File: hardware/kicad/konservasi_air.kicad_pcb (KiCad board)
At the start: 2 copper layers, 26 parts, among them J1 ADS1115, J10 PUMP, J11 DC_IN_TERMINAL, J2 DS18B20, J3 TDS, J4 TURBIDITY, J5 pH, J6 SERVO, J7 OLED, J8 ADS1115_ADDR_JP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

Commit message: PCB Layout Update
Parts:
- removed the SW1 at (66.0, 66.0)
- C1, C2: footprint Capacitor_THT:C_Disc_D7.5mm_W5.0mm_P7.50mm -> Capacitor_THT:C_Disc_D5.0mm_W2.5mm_P5.00mm
- D2: footprint Diode_THT:D_A-405_P12.70mm_Horizontal -> Diode_THT:D_DO-34_SOD68_P7.62mm_Horizontal
- J10: footprint Connector_PinSocket_2.54mm:PinSocket_1x02_P2.54mm_Vertical -> Connector_Molex:Molex_SL_171971-0002_1x02_P2.54mm_Vertical
- J8: value ADS1115_ADDR_JP -> ADS1115_ADDR
- R1, R2, R3, R4, R5: footprint Resistor_THT:R_Axial_DIN0309_L9.0mm_D3.2mm_P12.70mm_Horizontal -> Resistor_THT:R_Axial_DIN0204_L3.6mm_D1.6mm_P7.62mm_Horizontal
- SW1: renamed from SW2; footprint Connector_PinSocket_2.54mm:PinSocket_1x02_P2.54mm_Vertical -> Connector_Molex:Molex_SL_171971-0002_1x02_P2.54mm_Vertical
- moved J7 149.4 mm to (48.8, 118.6), turned to 90 degrees
- moved J6 143.2 mm to (48.8, 130.0), turned to 90 degrees
- moved D2 115.9 mm to (57.4, 135.9)
- moved Q1 98.2 mm to (60.8, 129.5)
- moved J4 78.4 mm to (119.7, 126.2), turned to -90 degrees
- moved J3 77.0 mm to (119.6, 114.6), turned to -90 degrees
- moved R5 74.8 mm to (66.0, 128.3), turned to -90 degrees
- moved J10 55.5 mm to (48.8, 138.9), turned to 90 degrees
- moved J11 53.0 mm to (63.2, 151.1), turned to 0 degrees
- moved SW1 45.1 mm to (48.8, 104.4), turned to 90 degrees
- moved R3 42.0 mm to (106.7, 115.3), turned to 90 degrees
- moved R4 41.0 mm to (109.0, 115.3), turned to 90 degrees
- moved C3 36.6 mm to (64.0, 140.7)
- moved C2 36.5 mm to (77.8, 151.6), turned to 0 degrees
- moved J9 36.3 mm to (50.6, 144.4)
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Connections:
- J8 pad 2: /ADS1115_ADDR -> GND
- J8 pad 4: /ADS1115_ADDR -> +5V
- J8 pad 5: GND -> /ADS1115_ADDR
- J8 pad 6: +5V -> /ADS1115_SDA
- J8 pad 7: /ADS1115_SDA -> /ADS1115_ADDR
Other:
- board outline added: 77.2 x 56.4 mm
- board text added: "OLED"
- board text added: "PH"
- board text added: "PUMP"
- board text added: "RESET"
- board text added: "SERVO"
- board text added: "TDS"
- board text added: "TEMP"
- board text added: "TURBIDITY"

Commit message: PCB Update
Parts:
- added J12: ESP_GPIO_LEFT, Connector_PinHeader_2.54mm:PinHeader_1x19_P2.54mm_Vertical, F.Cu at (68.6, 106.7)
- added J13: ESP_GPIO_RIGHT, Connector_PinHeader_2.54mm:PinHeader_1x19_P2.54mm_Vertical, F.Cu at (101.6, 106.7)
- moved R3 3.94 mm to (110.6, 115.6)
- moved R2 1.76 mm to (57.2, 145.8)
- moved D2 1.74 mm to (55.7, 135.9)
- moved C3 1.74 mm to (62.3, 140.7)
- moved C4 1.74 mm to (56.4, 140.7)
- moved D1 1.74 mm to (55.2, 151.9)
- moved J10 1.74 mm to (47.0, 138.9)
- moved J11 1.74 mm to (61.5, 151.1)
- moved J6 1.74 mm to (47.0, 130.0)
- moved J7 1.74 mm to (47.0, 118.6)
- moved J9 1.74 mm to (48.9, 144.4)
- moved Q1 1.74 mm to (59.0, 129.5)
- moved R5 1.74 mm to (64.3, 128.3)
- moved SW1 1.74 mm to (47.0, 104.4)
- moved R1 1.66 mm to (112.9, 108.0)
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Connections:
- net Net-(U1-CHIP_PU) renamed /ESP_RESET
- net Net-(U1-GPIO23) renamed /ESP_GPIO23
- U1 pad 10: unconnected-(U1-DAC_2/ADC2_CH9/GPIO26-Pad10) -> /ESP_GPIO26
- U1 pad 11: unconnected-(U1-ADC2_CH7/GPIO27-Pad11) -> /ESP_GPIO27
- U1 pad 12: unconnected-(U1-MTMS/GPIO14/ADC2_CH6-Pad12) -> /ESP_GPIO14
- U1 pad 13: unconnected-(U1-MTDI/GPIO12/ADC2_CH5-Pad13) -> /PUMP_DIGITAL
- U1 pad 15: unconnected-(U1-MTCK/GPIO13/ADC2_CH4-Pad15) -> /ESP_GPIO13
- U1 pad 16: unconnected-(U1-SD_DATA2/GPIO9-Pad16) -> /ESP_GPIO09
- U1 pad 17: unconnected-(U1-SD_DATA3/GPIO10-Pad17) -> /ESP_GPIO10
- U1 pad 18: unconnected-(U1-CMD-Pad18) -> /ESP_CMD
- U1 pad 20: unconnected-(U1-SD_CLK/GPIO6-Pad20) -> /ESP_GPIO06
- U1 pad 21: unconnected-(U1-SD_DATA0/GPIO7-Pad21) -> /ESP_GPIO07
- U1 pad 22: unconnected-(U1-SD_DATA1/GPIO8-Pad22) -> /ESP_GPIO08
- U1 pad 23: unconnected-(U1-MTDO/GPIO15/ADC2_CH3-Pad23) -> /ESP_GPIO15
- U1 pad 24: unconnected-(U1-ADC2_CH2/GPIO2-Pad24) -> /ESP_GPIO02
- U1 pad 25: unconnected-(U1-GPIO0/BOOT/ADC2_CH1-Pad25) -> /ESP_GPIO00
- U1 pad 26: unconnected-(U1-ADC2_CH0/GPIO4-Pad26) -> /ESP_GPIO04
- U1 pad 27: unconnected-(U1-GPIO16-Pad27) -> /ESP_GPIO16
- U1 pad 28: unconnected-(U1-GPIO17-Pad28) -> /ESP_GPIO17
- U1 pad 29: unconnected-(U1-GPIO5-Pad29) -> /ESP_GPIO05
- U1 pad 3: unconnected-(U1-SENSOR_VP/GPIO36/ADC1_CH0-Pad3) -> /ESP_GPIO36
- U1 pad 30: unconnected-(U1-GPIO18-Pad30) -> /ESP_GPIO18
- U1 pad 34: unconnected-(U1-U0RXD/GPIO3-Pad34) -> /ESP_GPIO03
- U1 pad 35: unconnected-(U1-U0TXD/GPIO1-Pad35) -> /ESP_GPIO01
- U1 pad 4: unconnected-(U1-SENSOR_VN/GPIO39/ADC1_CH3-Pad4) -> /ESP_GPIO39
- U1 pad 5: unconnected-(U1-VDET_1/GPIO34/ADC1_CH6-Pad5) -> /ESP_GPIO34
- U1 pad 6: unconnected-(U1-VDET_2/GPIO35/ADC1_CH7-Pad6) -> /ESP_GPIO35
- U1 pad 7: unconnected-(U1-32K_XP/GPIO32/ADC1_CH4-Pad7) -> /ESP_GPIO32
- U1 pad 8: unconnected-(U1-32K_XN/GPIO33/ADC1_CH5-Pad8) -> /ESP_GPIO33
- U1 pad 9: unconnected-(U1-DAC_1/ADC2_CH8/GPIO25-Pad9) -> /ESP_GPIO25
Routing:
- added copper zone on B.Cu, net GND
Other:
- board size 77.2 x 56.4 mm -> 81.5 x 56.4 mm

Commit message: Done Routing
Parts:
- removed J8: ADS1115_ADDR, Connector_PinHeader_2.54mm:PinHeader_2x04_P2.54mm_Vertical
- added JP1: ADS1115_ADDR_5V, Jumper:SolderJumper-2_P1.3mm_Open_RoundedPad1.0x1.5mm, B.Cu at (113.1, 116.9)
- added JP2: ADS1115_ADDR_SDA, Jumper:SolderJumper-2_P1.3mm_Open_RoundedPad1.0x1.5mm, B.Cu at (108.5, 116.9)
- added JP3: ADS1115_ADDR_SCL, Jumper:SolderJumper-2_P1.3mm_Open_RoundedPad1.0x1.5mm, B.Cu at (110.8, 116.9)
- J9: value DC_IN_JACK -> Barrel_Jack_Switch
- moved C3 2.02 mm to (64.3, 140.7), turned to 180 degrees
- moved C4 2.00 mm to (58.4, 140.7), turned to 180 degrees
- moved R4 1.75 mm to (108.5, 113.8)
- moved R1 1.74 mm to (113.1, 106.2)
- moved R3 1.74 mm to (110.8, 113.8)
- moved J1 1.73 mm to (105.5, 106.7)
- moved C2 0.51 mm to (77.8, 152.1), turned to 90 degrees
- moved D1 0.51 mm to (55.2, 152.4)
- moved J9 0.25 mm to (48.6, 144.4)
- moved R5 0.25 mm to (64.3, 128.5)
- moved D2 0.25 mm to (55.7, 136.1)
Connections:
- J13 pad 8: /SERVO_PWM -> /ESP_GPIO19
- J6 pad 1: /SERVO_PWM -> /ESP_GPIO25
- J7 pad 3: /ADS1115_SCL -> /ADS1115_SDA
- J7 pad 4: /ADS1115_SDA -> /ADS1115_SCL
- J9 pad 3: (no net) -> unconnected-(J9-Pad3)
- U1 pad 31: /SERVO_PWM -> /ESP_GPIO19
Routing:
- net +5V: track 0.00 -> 120.7 mm
- net /ADS1115_SDA: track 0.00 -> 74.0 mm
- net /ADS1115_SCL: track 0.00 -> 68.5 mm
- net /PH_ANALOG: track 0.00 -> 32.6 mm
- net /ESP_RESET: track 0.00 -> 27.4 mm
- net /ESP_GPIO25: track 0.00 -> 26.7 mm
- net /TDS_ANALOG: track 0.00 -> 21.6 mm
- net /PUMP_GND: track 0.00 -> 17.8 mm
- net /ESP_GPIO23: track 0.00 -> 17.2 mm
- net /TURBIDITY_ANALOG: track 0.00 -> 16.6 mm
- net /DS18B20_DIGITAL: track 0.00 -> 16.5 mm
- net GND: track 0.00 -> 11.4 mm
- net +3V3: track 0.00 -> 9.25 mm
- net /PUMP_DIGITAL: track 0.00 -> 8.80 mm
- net /ADS1115_ADDR: track 0.00 -> 7.97 mm
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- added copper zone on F.Cu, net GND
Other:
- board size 81.5 x 56.4 mm -> 81.5 x 58.7 mm

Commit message: PCB Modified
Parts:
- added REF**: MountingHole_3.2mm_M3_DIN965_Pad, MountingHole:MountingHole_3.2mm_M3_DIN965_Pad, F.Cu at (113.1, 149.9)
- added REF**: MountingHole_3.2mm_M3_DIN965_Pad, MountingHole:MountingHole_3.2mm_M3_DIN965_Pad, F.Cu at (57.2, 101.6)
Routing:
- net +5V: track 120.7 -> 235.3 mm
- net /ADS1115_SDA: track 74.0 -> 72.4 mm
- net /ADS1115_SCL: track 68.5 -> 69.2 mm
- net GND: vias 0 -> 111
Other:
- outline, holes or cut-outs redrawn
- board text added: "- +"

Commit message: Update PCB
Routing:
- net +5V: track 235.3 -> 236.2 mm
- net GND: vias 111 -> 124
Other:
- board text added: "+5V"
- board text added: "AOUT"
- board text added: "DOUT"
- board text added: "GND"
- board text added: "MOT_A"
- board text added: "MOT_B"
- board text added: "PWM"
- board text added: "RST"
- board text added: "SCL"
- board text added: "SDA"

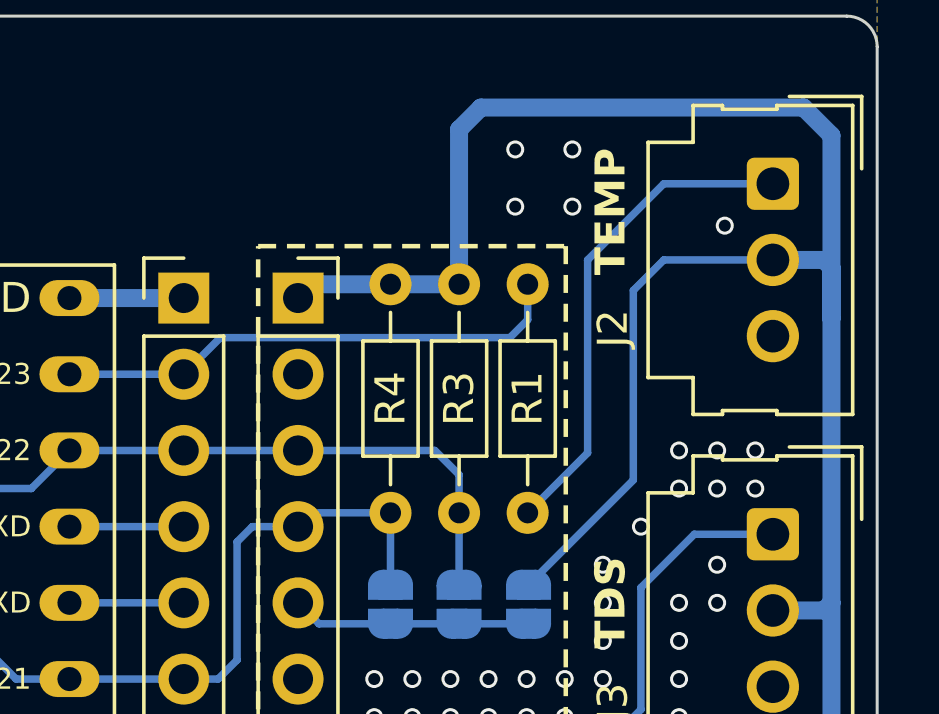
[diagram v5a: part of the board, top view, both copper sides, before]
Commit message: Fix Pullup for Temp Sensor
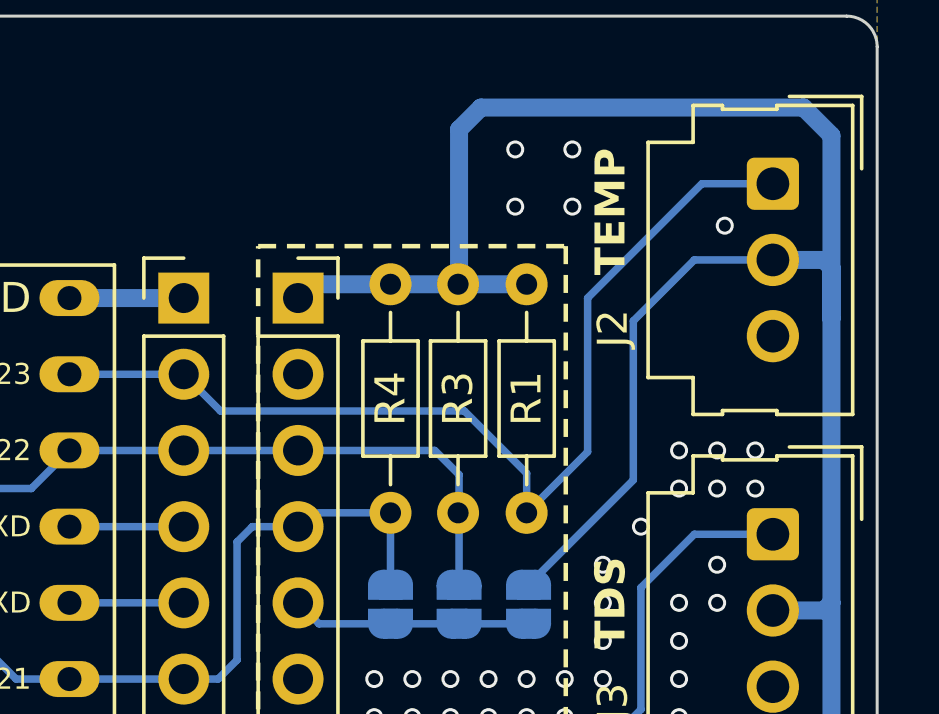
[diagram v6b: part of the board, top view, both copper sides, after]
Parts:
- moved R1 7.62 mm to (113.1, 113.8), turned to 90 degrees
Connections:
- J13 pad 2: /ESP_GPIO23 -> /DS18B20_DIGITAL
- R1 pad 1: /ESP_GPIO23 -> /DS18B20_DIGITAL
- R1 pad 2: /DS18B20_DIGITAL -> +5V
- REF** pad 1: (no net) -> GND (x2)
- U1 pad 37: /ESP_GPIO23 -> /DS18B20_DIGITAL
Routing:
- net /ESP_GPIO23: track 17.2 -> 0.00 mm
- net /DS18B20_DIGITAL: track 16.5 -> 33.7 mm
- net +5V: track 236.2 -> 237.9 mm

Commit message: Update konservasi_air.kicad_pcb
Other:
- board text added: "Design Proyek - Konservasi Air"
- board text added: "Kelompok 1.9 - Nov 2023"
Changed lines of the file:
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@@
     (effects (font (size 1 1) (thickness 0.15)) (justify left bottom mirror))
+  )
+  (gr_text "Kelompok 1.9 - Nov 2023" (at 108.752 103.886) (layer "B.SilkS")
+    (effects (font (size 1 1) (thickness 0.15)) (justify left bottom mirror))
+  )
+  (gr_text "Design Proyek - Konservasi Air" (at 90.718 100.076) (layer "B.SilkS" knockout)
+    (effects (font (size 1.5 1.5) (thickness 0.3)) (justify mirror))
   )
   (gr_text "DOUT" (at 119.674 103.632) (layer "B.SilkS")
